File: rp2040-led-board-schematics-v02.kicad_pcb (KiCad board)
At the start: 4 copper layers, 230 x 98 mm, 257 parts, among them J1 PWR_IN, J10 ReceiverData, J11 ReceiverRS485, J12 ReceiverData, J13 MainBoard, J14 Terminal, J15 Terminal, J16 Terminal, J17 Terminal, J18 Terminal, J19 Terminal, J2 Terminal, J20 Terminal, J21 ReceiverRS485, J22 ReceiverData, J23 ReceiverRS485, J24 ReceiverData, J25 ReceiverRS485, J26 ReceiverData, J27 ReceiverRS485, J3 ReceiverData, J4 ReceiverRS485, J5 FrontPanel, J6 ReceiverData, J7 ReceiverRS485, J8 ReceiverData, J9 ReceiverRS485, SW1 Button, SW2 PEC16, U1 LM7805, U10 MAX485E, U11 MAX485E, U12 ENC28J60, U13 LM7805, U14 MAX485E, U15 LM7805, U16 MAX485E, U17 LM7805, U18 MAX485E, U19 LM7805, U2 MAX485E, U20 MAX485E, U21 LM7805, U22 MAX485E, U23 LM7805, U24 MAX485E, U25 LM7805, U26 MAX485E, U27 LM7805, U3 MAX485E, U4 MAX485E, U5 MAX485E, U6 MAX485E, U7 Pico, U8 MAX485E, U9 MAX485E

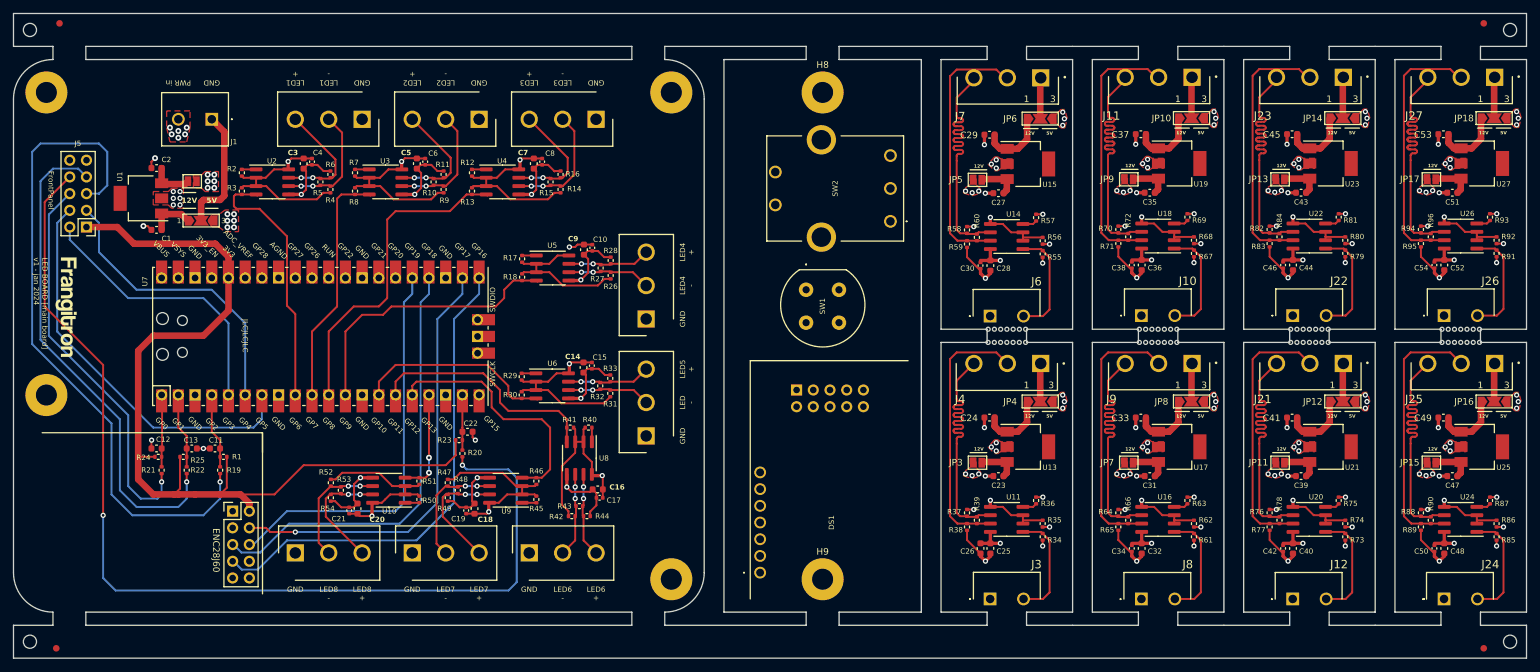
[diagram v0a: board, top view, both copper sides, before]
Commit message: panelization with only mouse bites, routing finished
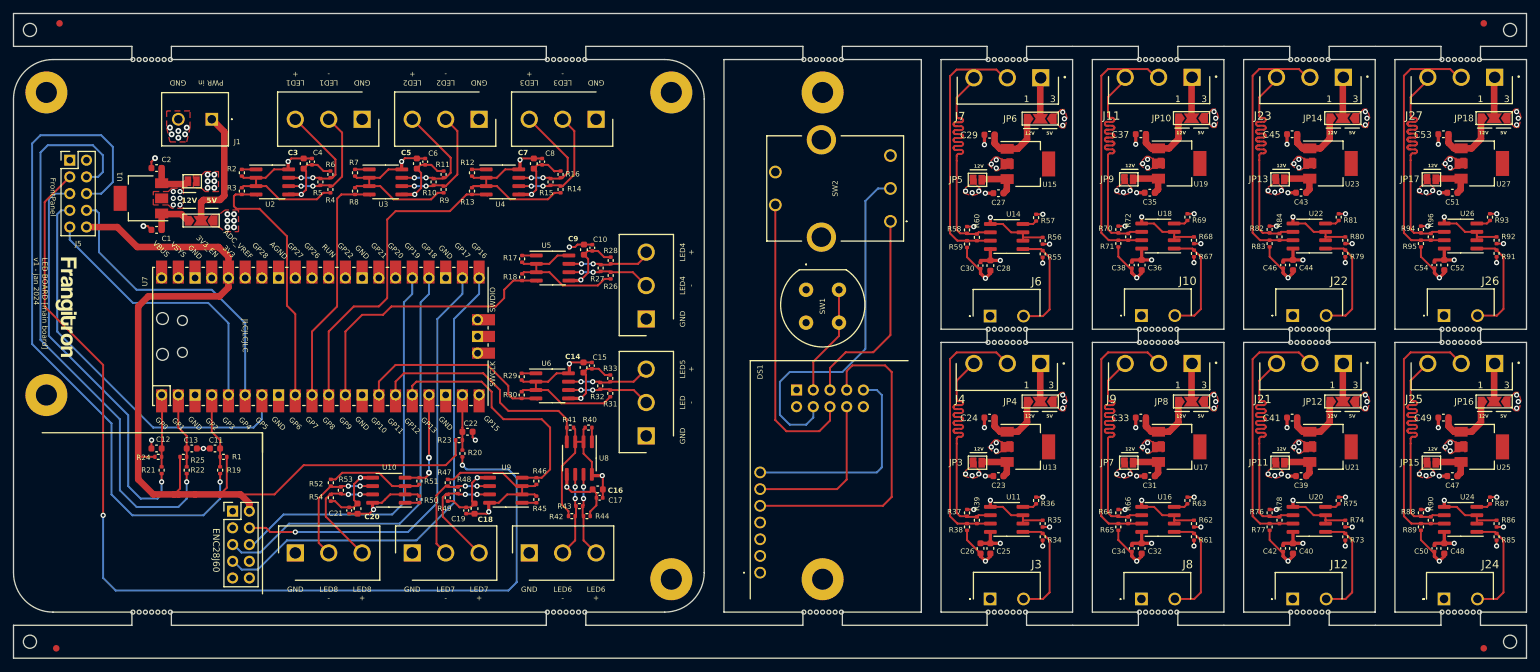
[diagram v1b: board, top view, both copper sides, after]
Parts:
- added H29: ~, Library:mouse-bites-1x07-jlc, F.Cu at (161.0, 140.0)
- added H30: ~, Library:mouse-bites-1x07-jlc, F.Cu at (161.0, 56.0)
- added H31: ~, Library:mouse-bites-1x07-jlc, F.Cu at (59.0, 56.0)
- added H32: ~, Library:mouse-bites-1x07-jlc, F.Cu at (122.0, 56.0)
- added H33: ~, Library:mouse-bites-1x07-jlc, F.Cu at (59.0, 140.0)
- added H34: ~, Library:mouse-bites-1x07-jlc, F.Cu at (122.0, 140.0)
- added H35: ~, Library:mouse-bites-1x07-jlc, F.Cu at (189.0, 140.0)
- added H36: ~, Library:mouse-bites-1x07-jlc, F.Cu at (189.0, 56.0)
- added H37: ~, Library:mouse-bites-1x07-jlc, F.Cu at (212.0, 140.0)
- added H38: ~, Library:mouse-bites-1x07-jlc, F.Cu at (212.0, 56.0)
- added H39: ~, Library:mouse-bites-1x07-jlc, F.Cu at (235.0, 140.0)
- added H40: ~, Library:mouse-bites-1x07-jlc, F.Cu at (235.0, 56.0)
- added H41: ~, Library:mouse-bites-1x07-jlc, F.Cu at (258.0, 140.0)
- added H42: ~, Library:mouse-bites-1x07-jlc, F.Cu at (258.0, 56.0)
- moved J5 10.5 mm to (46.6, 71.3), turned to 0 degrees
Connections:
- DS1 pad 1: FP GND -> /FP GND
- DS1 pad 2: FP +3V3 -> /FP +3V3
- DS1 pad 3: FP +3V3 -> /FP +3V3
- DS1 pad 4: FP GND -> /FP GND
- H8 pad 1: FP GND -> /FP GND
- H9 pad 1: FP GND -> /FP GND
- J13 pad 1: FP +3V3 -> /FP GND
- J13 pad 10: FP GND -> /FP +3V3
- J13 pad 2: FPDisplayRST -> unconnected-(J13-Pin_2-Pad2)
- J13 pad 3: FPDisplaySDA -> FPSwitchPush
- J13 pad 4: FPDisplaySCL -> FPEncoderB
- J13 pad 5: FPEncoderS -> FPEncoderA
- J13 pad 6: FPEncoderA -> FPEncoderS
- J13 pad 7: FPEncoderB -> FPDisplaySCL
- J13 pad 8: FPSwitchPush -> FPDisplaySDA
- J13 pad 9: unconnected-(J13-Pin_9-Pad9) -> FPDisplayRST
- J24 pad 1: (no net) -> /Receiver 7/GND
- J24 pad 2: (no net) -> /Receiver 7/DATA
- J5 pad 1: +3V3 -> GND
- J5 pad 10: GND -> +3V3
- J5 pad 2: MCUDisplayRST -> unconnected-(J5-Pin_2-Pad2)
- J5 pad 3: MCUDisplaySDA -> MBSwitchPush
- J5 pad 4: MCUDisplaySCL -> MBEncoderB
- J5 pad 5: MBEncoderS -> MBEncoderA
- J5 pad 6: MBEncoderA -> MBEncoderS
- J5 pad 7: MBEncoderB -> MCUDisplaySCL
- J5 pad 8: MBSwitchPush -> MCUDisplaySDA
- J5 pad 9: unconnected-(J5-Pin_9-Pad9) -> MCUDisplayRST
- SW1 pad 1: unconnected-(SW1-Pad1) -> /FP GND
- SW1 pad 2: FP GND -> /FP GND
- SW1 pad 4: unconnected-(SW1-A-Pad4) -> FPSwitchPush
- SW2 pad C1: FP GND -> /FP GND
- SW2 pad E1: FP GND -> /FP GND
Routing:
- net FPEncoderB: track 0.00 -> 55.0 mm
- net FPDisplaySCL: track 0.00 -> 50.1 mm
- net FPEncoderS: track 0.00 -> 44.5 mm
- net FPDisplayRST: track 0.00 -> 32.9 mm
- net FPEncoderA: track 0.00 -> 31.9 mm
- net FPDisplaySDA: track 0.00 -> 24.8 mm
- net FPSwitchPush: track 0.00 -> 16.9 mm
- net MBEncoderB: track 75.8 -> 87.8 mm
- net MBEncoderS: track 101.0 -> 104.6 mm
- net +3V3: track 140.3 -> 142.2 mm
- net MBEncoderA: track 60.1 -> 61.4 mm
- net MCUDisplaySDA: track 44.7 -> 45.6 mm
- net MCUDisplaySCL: track 60.6 -> 61.4 mm
- net +5V: track 234.2 -> 233.6 mm
- added copper zone on In2.Cu, net /FP +3V3
- added copper zone on In1.Cu, net /FP GND
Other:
- outline, holes or cut-outs redrawn

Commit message: resize front panel, fix header orientation, fix receivers layouts and footprints
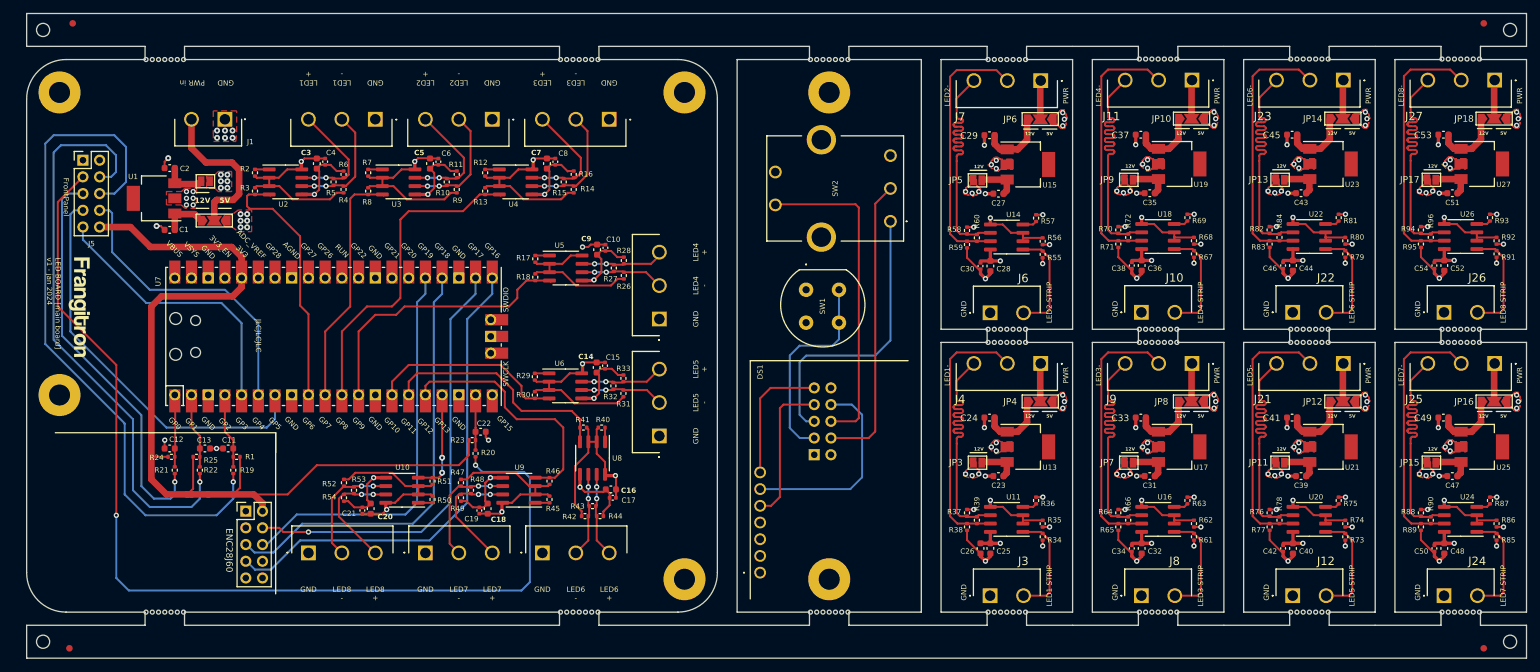
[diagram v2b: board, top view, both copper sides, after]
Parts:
- moved H24 41.1 mm to (258.0, 55.9), turned to 0 degrees
- moved H16 41.1 mm to (212.0, 55.9), turned to 0 degrees
- moved H20 41.1 mm to (235.0, 55.9), turned to 0 degrees
- moved H36 41.0 mm to (189.0, 97.0)
- moved H42 41.0 mm to (258.0, 97.0)
- moved H38 41.0 mm to (212.0, 97.0)
- moved H40 41.0 mm to (235.0, 97.0)
- moved H12 41.0 mm to (189.0, 56.0), turned to 0 degrees
- moved J13 10.2 mm to (159.7, 116.1), turned to 0 degrees
- moved U12 2.00 mm to (75.9, 129.7)
- moved FM1 2.00 mm to (47.0, 50.5)
- moved FM4 2.00 mm to (46.5, 145.5)
- moved H25 2.00 mm to (42.5, 51.5)
- moved H26 2.00 mm to (42.5, 144.5)
- moved R32 2.00 mm to (129.2, 105.6)
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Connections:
- J1 pad 1: Net-(J1-Pin_1) -> GND
- J1 pad 2: GND -> Net-(J1-Pin_2)
- JP2 pad 2: Net-(J1-Pin_1) -> Net-(J1-Pin_2)
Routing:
- net FPDisplaySCL: track 50.1 -> 22.5 mm
- net Net-(J1-Pin_2): track 0.00 -> 23.8 mm
- net Net-(J1-Pin_1): track 19.2 -> 0.00 mm
- net FPSwitchPush: track 16.9 -> 31.4 mm
- net FPDisplayRST: track 32.9 -> 20.1 mm
- net FPEncoderA: track 31.9 -> 43.9 mm
- net FPEncoderB: track 55.0 -> 45.0 mm
- net FPDisplaySDA: track 24.8 -> 31.1 mm
- net FPEncoderS: track 44.5 -> 49.4 mm
- net /Receiver 2/DATA: track 16.9 -> 16.1 mm
- net /Receiver 6/DATA: track 16.9 -> 16.2 mm
- net /Receiver 4/DATA: track 16.9 -> 16.2 mm
- net /Receiver 8/DATA: track 16.9 -> 16.2 mm
- net /Receiver 3/DATA: track 16.9 -> 16.2 mm
- net /Receiver 7/DATA: track 16.9 -> 16.2 mm
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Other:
- board size 230 x 98 mm -> 228 x 98 mm
- board text added: "LED1 STRIP"
- board text added: "LED1-"
- board text added: "LED2 STRIP"
- board text added: "LED2-"
- board text added: "LED3 STRIP"
- board text added: "LED3-"
- board text added: "LED4 STRIP"
- board text added: "LED4-"
- board text added: "LED5 -"
- board text added: "LED5 STRIP"
- board text added: "LED5-"
- board text added: "LED6 STRIP"
- board text added: "LED6-"
- board text added: "LED7 STRIP"
- board text added: "LED7-"
- board text added: "LED8 STRIP"
- board text added: "LED8-"
- board text added: "PWR"
- board text removed: "LED -"
- board text removed: "locked"

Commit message: Geographically reannotate
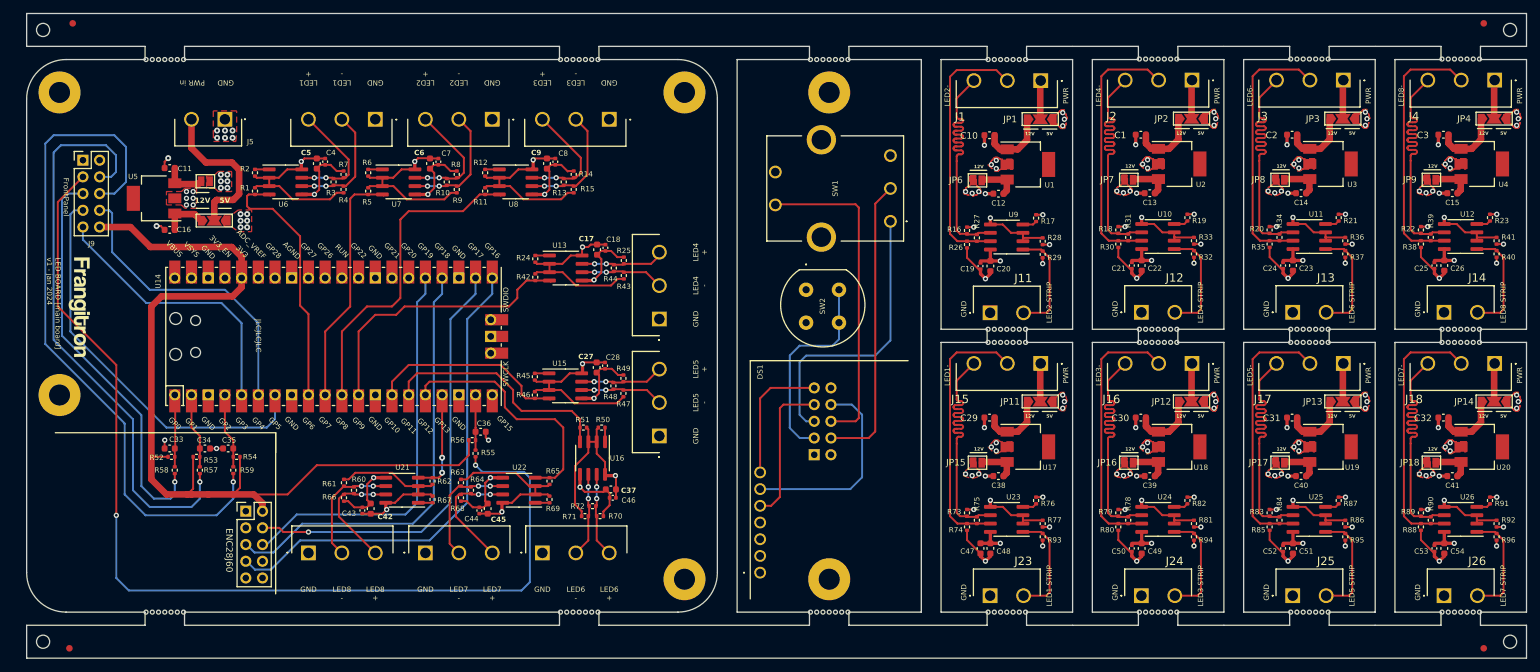
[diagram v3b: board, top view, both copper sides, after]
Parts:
- renumbered C37 to C1, C29 to C10, C2 to C11, C27 to C12, C35 to C13, C43 to C14, C51 to C15, C1 to C16, C9 to C17, C10 to C18, C30 to C19, C45 to C2, C28 to C20, C38 to C21, C36 to C22, C44 to C23, C46 to C24, C54 to C25, C52 to C26, C14 to C27, C15 to C28, C24 to C29, C53 to C3, C33 to C30, C41 to C31, C49 to C32, C12 to C33, C13 to C34, C11 to C35, C22 to C36, C16 to C37, C23 to C38, C31 to C39, C39 to C40, C47 to C41, C20 to C42, C21 to C43, C19 to C44, C18 to C45, C17 to C46, C26 to C47, C25 to C48, C32 to C49, C3 to C5, C34 to C50, C40 to C51, C42 to C52, C50 to C53, C48 to C54, C5 to C6, C6 to C7, C7 to C9, FM4 to FM3, FM3 to FM4, H25 to H1, H1 to H10, H2 to H11, H8 to H12, H3 to H13, H36 to H14, H38 to H15, H40 to H16, H42 to H17, H11 to H18, H14 to H19, H28 to H2, H18 to H20, H22 to H21, H4 to H22, H5 to H23, H9 to H24, H33 to H25, H34 to H26, H29 to H27, H35 to H28, H37 to H29, H31 to H3, H39 to H30, H41 to H31, H26 to H32, H27 to H33, H23 to H34, H19 to H35, H15 to H36, H10 to H37, H21 to H38, H17 to H39, H32 to H4, H13 to H40, H7 to H41, H6 to H42, H30 to H5, H12 to H6, H16 to H7, H20 to H8, H24 to H9, J7 to J1, J16 to J10, J6 to J11, J10 to J12, J22 to J13, J26 to J14, J4 to J15, J9 to J16, J21 to J17, J25 to J18, J17 to J19, J11 to J2, J19 to J21, J18 to J22, J3 to J23, J8 to J24, J12 to J25, J24 to J26, J13 to J27, J23 to J3, J27 to J4, J1 to J5, J2 to J6, J14 to J7, J15 to J8, J5 to J9, JP6 to JP1, JP2 to JP10, JP4 to JP11, JP8 to JP12, JP12 to JP13, JP16 to JP14, JP3 to JP15, JP7 to JP16, JP11 to JP17, JP15 to JP18, JP10 to JP2, JP14 to JP3, JP18 to JP4, JP1 to JP5, JP5 to JP6, JP9 to JP7, JP13 to JP8, JP17 to JP9, R3 to R1, R13 to R11, R15 to R13, R16 to R14, R14 to R15, R58 to R16, R57 to R17, R70 to R18, R69 to R19, R82 to R20, R81 to R21, R94 to R22, R93 to R23, R17 to R24, R28 to R25, R59 to R26, R60 to R27, R56 to R28, R55 to R29, R5 to R3, R71 to R30, R72 to R31, R67 to R32, R68 to R33, R84 to R34, R83 to R35, R80 to R36, R79 to R37, R95 to R38, R96 to R39, R91 to R40, R92 to R41, R18 to R42, R26 to R43, R27 to R44, R29 to R45, R30 to R46, R31 to R47, R32 to R48, R33 to R49, R8 to R5, R40 to R50, R41 to R51, R24 to R52, R25 to R53, R1 to R54, R20 to R55, R23 to R56, R22 to R57, R21 to R58, R19 to R59, R7 to R6, R53 to R60, R52 to R61, R51 to R62, R47 to R63, R48 to R64, R46 to R65, R54 to R66, R50 to R67, R49 to R68, R45 to R69, R6 to R7, R44 to R70, R42 to R71, R43 to R72, R37 to R73, R38 to R74, R39 to R75, R36 to R76, R35 to R77, R66 to R78, R64 to R79, R11 to R8, R65 to R80, R62 to R81, R63 to R82, R76 to R83, R78 to R84, R77 to R85, R74 to R86, R75 to R87, R89 to R88, R88 to R89, R87 to R91, R86 to R92, R34 to R93, R61 to R94, R73 to R95, R85 to R96, SW2 to SW1, SW1 to SW2, U15 to U1, U18 to U10, U22 to U11, U26 to U12, U5 to U13, U7 to U14, U6 to U15, U8 to U16, U13 to U17, U17 to U18, U21 to U19, U19 to U2, U25 to U20, U10 to U21, U9 to U22, U11 to U23, U16 to U24, U20 to U25, U24 to U26, U12 to U27, U23 to U3, U27 to U4, U1 to U5, U2 to U6, U3 to U7, U4 to U8, U14 to U9
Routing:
- net +5V: track 233.6 -> 234.9 mm

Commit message: fix power sources, update reveivers accordingly (main board PCB not updated yet)
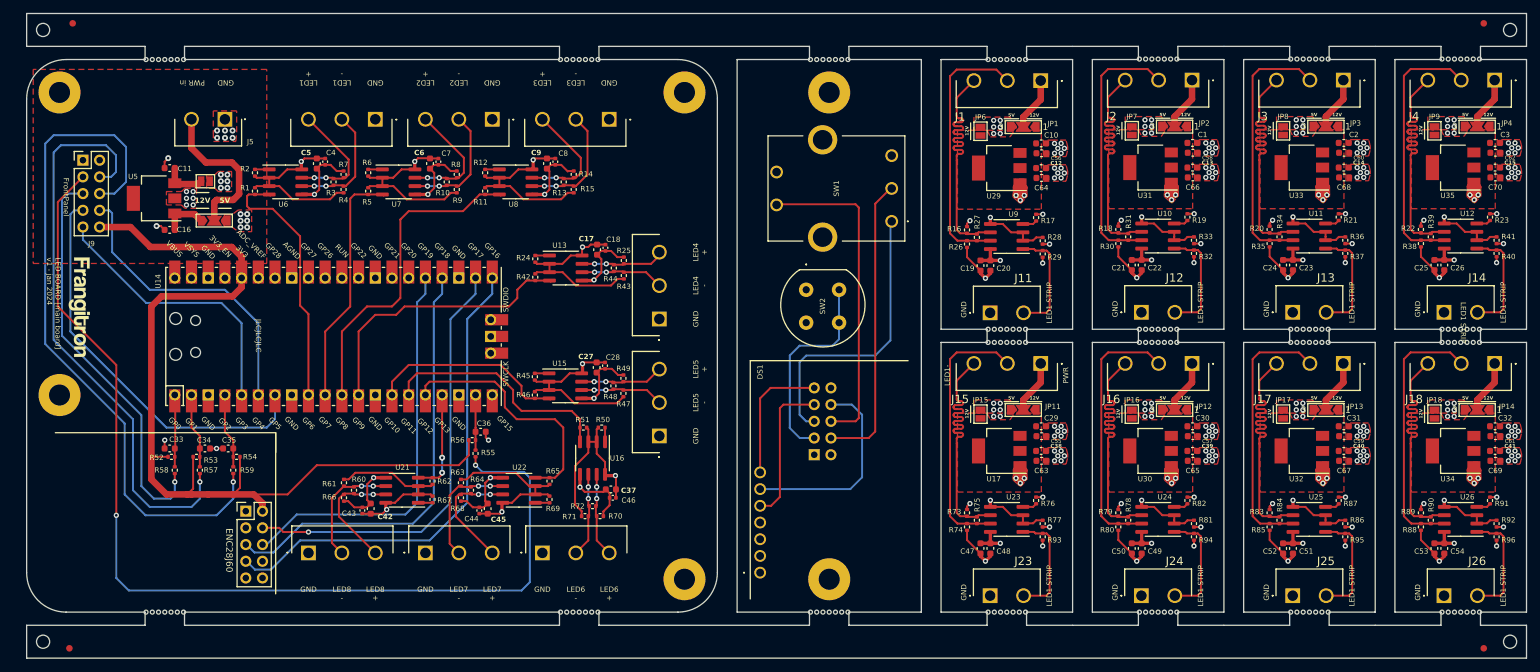
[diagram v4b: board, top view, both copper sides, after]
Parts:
- removed U1, U18, U19, U2, U20, U3, U4: LM7805, Package_TO_SOT_SMD:SOT-223
- added C55: 100nF, Capacitor_SMD:C_0603_1608Metric, F.Cu at (194.3, 113.2)
- added C56: 100nF, Capacitor_SMD:C_0603_1608Metric, F.Cu at (194.3, 70.2)
- added C57: 100nF, Capacitor_SMD:C_0603_1608Metric, F.Cu at (217.3, 113.2)
- added C58: 100nF, Capacitor_SMD:C_0603_1608Metric, F.Cu at (217.3, 70.2)
- added C59: 100nF, Capacitor_SMD:C_0603_1608Metric, F.Cu at (240.3, 113.2)
- added C60: 100nF, Capacitor_SMD:C_0603_1608Metric, F.Cu at (240.3, 70.2)
- added C61: 100nF, Capacitor_SMD:C_0603_1608Metric, F.Cu at (263.3, 113.2)
- added C62: 100nF, Capacitor_SMD:C_0603_1608Metric, F.Cu at (263.3, 70.2)
- added C63: 100nF, Capacitor_SMD:C_0603_1608Metric, F.Cu at (194.3, 117.0)
- added C64: 100nF, Capacitor_SMD:C_0603_1608Metric, F.Cu at (194.3, 74.0)
- added C65: 100nF, Capacitor_SMD:C_0603_1608Metric, F.Cu at (217.3, 117.0)
- added C66: 100nF, Capacitor_SMD:C_0603_1608Metric, F.Cu at (217.3, 73.9)
- added C67: 100nF, Capacitor_SMD:C_0603_1608Metric, F.Cu at (240.3, 117.0)
- added C68: 100nF, Capacitor_SMD:C_0603_1608Metric, F.Cu at (240.3, 73.9)
- added C69: 100nF, Capacitor_SMD:C_0603_1608Metric, F.Cu at (263.3, 117.0)
- added C70: 100nF, Capacitor_SMD:C_0603_1608Metric, F.Cu at (263.3, 73.9)
- added U29: AMS1117-5.0, Package_TO_SOT_SMD:SOT-223-3_TabPin2, F.Cu at (187.8, 72.5)
- added U30: AMS1117-5.0, Package_TO_SOT_SMD:SOT-223-3_TabPin2, F.Cu at (210.8, 115.5)
- added U31: AMS1117-5.0, Package_TO_SOT_SMD:SOT-223-3_TabPin2, F.Cu at (210.8, 72.4)
- added U32: AMS1117-5.0, Package_TO_SOT_SMD:SOT-223-3_TabPin2, F.Cu at (233.8, 115.5)
- added U33: AMS1117-5.0, Package_TO_SOT_SMD:SOT-223-3_TabPin2, F.Cu at (233.8, 72.4)
- added U34: AMS1117-5.0, Package_TO_SOT_SMD:SOT-223-3_TabPin2, F.Cu at (256.8, 115.5)
- added U35: AMS1117-5.0, Package_TO_SOT_SMD:SOT-223-3_TabPin2, F.Cu at (256.8, 72.4)
- C1, C10, C2, C29, C3, C30, C31, C32: value 220nF -> 10uF
- C12, C13, C14, C15, C38, C39, C40, C41: value 100nF -> 10uF
- C19, C21, C24, C25, C50, C52, C53: footprint Capacitor_SMD:C_0402_1005Metric -> Capacitor_SMD:C_0603_1608Metric
- U10, U11, U12, U13, U15, U16, U21, U22, U23, U24, U25, U26, U6, U7, U8, U9: value MAX485E -> MAX485EE
- U17: value LM7805 -> AMS1117-5.0; footprint Package_TO_SOT_SMD:SOT-223 -> Package_TO_SOT_SMD:SOT-223-3_TabPin2
- U5: value LM7805 -> NCP1117LP
- moved C32 7.97 mm to (263.2, 111.8), turned to 0 degrees
- moved C29 7.97 mm to (194.2, 111.8), turned to 0 degrees
- moved C30 7.97 mm to (217.2, 111.8), turned to 0 degrees
- moved C31 7.97 mm to (240.2, 111.8), turned to 0 degrees
- moved C3 7.95 mm to (263.2, 68.7), turned to 0 degrees
- moved C1 7.95 mm to (217.2, 68.7), turned to 0 degrees
- moved C10 7.95 mm to (194.2, 68.8), turned to 0 degrees
- moved C2 7.95 mm to (240.2, 68.7), turned to 0 degrees
- moved H39 7.62 mm to (231.5, 113.0), turned to 90 degrees
- moved H38 7.62 mm to (254.5, 113.0), turned to 90 degrees
- moved H40 7.62 mm to (208.5, 113.0), turned to 90 degrees
- moved H41 7.62 mm to (185.5, 113.0), turned to 90 degrees
- moved C12 7.57 mm to (194.2, 72.5), turned to 0 degrees
- moved C13 7.57 mm to (217.2, 72.4), turned to 0 degrees
- moved C14 7.57 mm to (240.2, 72.4), turned to 0 degrees
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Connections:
- net Net-(JP11-B) renamed /Receiver 5/LDO OUT
- net Net-(JP13-B) renamed /Receiver 6/LDO OUT
- net Net-(JP15-B) renamed /Receiver 7/LDO OUT
- net Net-(JP17-B) renamed /Receiver 8/LDO OUT
- net Net-(JP5-B) renamed /Receiver 2/LDO OUT
- net Net-(JP7-B) renamed /Receiver 3/LDO OUT
- net Net-(JP9-B) renamed /Receiver 4/LDO OUT
- C38 pad 1: Net-(JP3-B) -> /Receiver 1/LDO OUT
- JP15 pad 2: Net-(JP3-B) -> /Receiver 1/LDO OUT
- U17 pad 1: /Receiver 1/12V -> /Receiver 1/GND
- U17 pad 2: /Receiver 1/GND -> /Receiver 1/LDO OUT
- U17 pad 3: Net-(JP3-B) -> /Receiver 1/12V
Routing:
- net /Receiver 8/12V: track 10.3 -> 0.00 mm
- net /Receiver 7/12V: track 10.3 -> 0.00 mm
- net /Receiver 2/12V: track 10.3 -> 0.00 mm
- net /Receiver 6/12V: track 10.3 -> 0.00 mm
- net /Receiver 4/12V: track 10.3 -> 0.00 mm
- net /Receiver 3/12V: track 10.3 -> 0.00 mm
- net /Receiver 1/12V: track 10.3 -> 0.00 mm
- net /Receiver 5/12V: track 10.3 -> 0.00 mm
- net Net-(JP3-B): track 6.28 -> 0.00 mm
- net /Receiver 7/LDO OUT: track 6.28 -> 0.00 mm
- net /Receiver 5/LDO OUT: track 6.28 -> 0.00 mm
- net /Receiver 8/LDO OUT: track 6.28 -> 0.00 mm
- net /Receiver 3/LDO OUT: track 6.28 -> 0.00 mm
- net /Receiver 2/LDO OUT: track 6.28 -> 0.00 mm
- net /Receiver 6/LDO OUT: track 6.28 -> 0.00 mm
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- added copper zone on F.Cu, net /Receiver 1/LDO OUT
- added copper zone on F.Cu, net /Receiver 2/LDO OUT
- added copper zone on F.Cu, net /Receiver 3/LDO OUT
- added copper zone on F.Cu, net /Receiver 4/LDO OUT
- added copper zone on F.Cu, net /Receiver 5/LDO OUT
- added copper zone on F.Cu, net /Receiver 6/LDO OUT
- added copper zone on F.Cu, net /Receiver 7/LDO OUT
- added copper zone on F.Cu, net /Receiver 8/LDO OUT
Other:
- board text removed: "LED2 STRIP"
- board text removed: "LED2-"
- board text removed: "LED3 STRIP"
- board text removed: "LED3-"
- board text removed: "LED4 STRIP"
- board text removed: "LED4-"
- board text removed: "LED5 STRIP"
- board text removed: "LED5-"
- board text removed: "LED6 STRIP"
- board text removed: "LED6-"
- board text removed: "LED7 STRIP"
- board text removed: "LED7-"
- board text removed: "LED8 STRIP"
- board text removed: "LED8-"
